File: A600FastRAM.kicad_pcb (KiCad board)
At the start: 2 copper layers, 92.7 x 78.7 mm, 22 parts, among them J1 MC68000_PLCC68, P1 JTAG_CONNECTOR, P98 SCREW_HOLE, P99 OSHW_LOGO, U1 74LS157, U2 74LS157, U3 HYB5118160BSJ, U4 HYB5118160BSJ, U5 ATF1502AS-10JU44

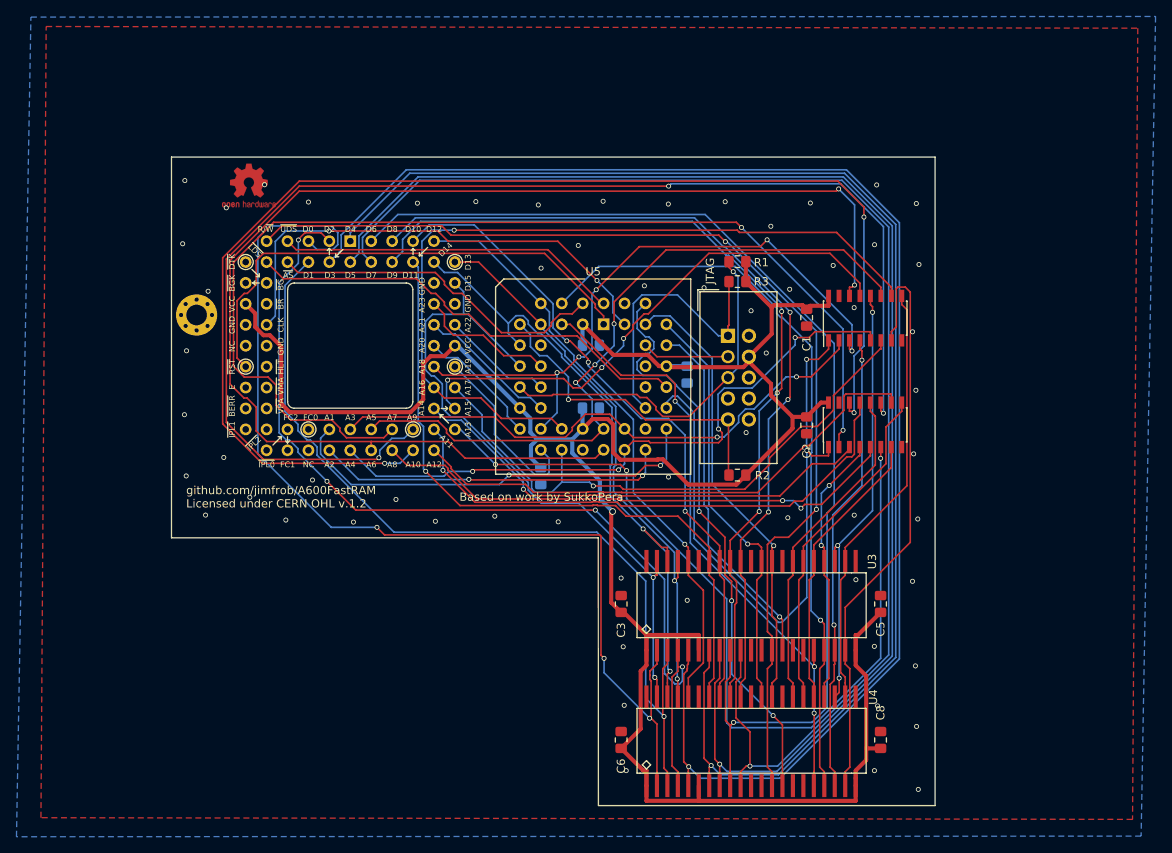
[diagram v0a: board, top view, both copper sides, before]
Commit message: rounded the corners of the PCB
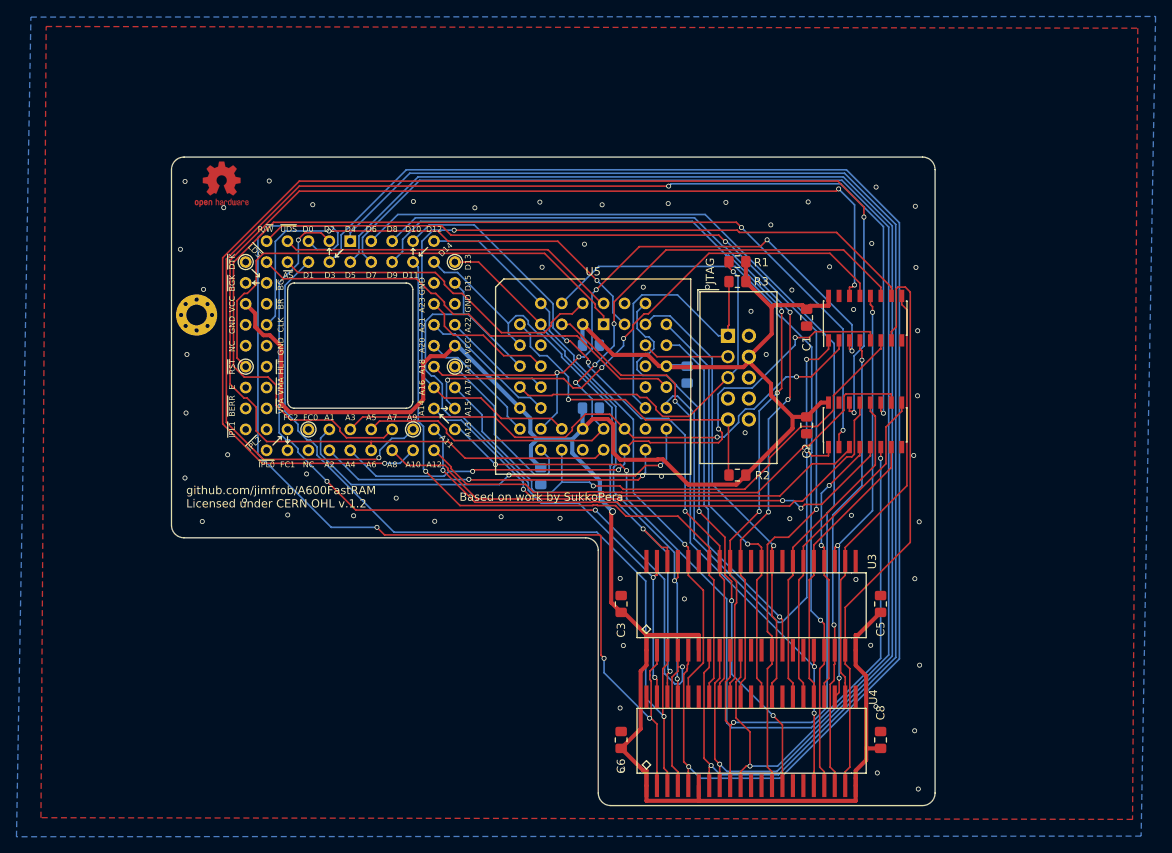
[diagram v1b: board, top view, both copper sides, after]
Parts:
- moved P99 3.31 mm to (117.1, 86.1)
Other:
- outline, holes or cut-outs redrawn

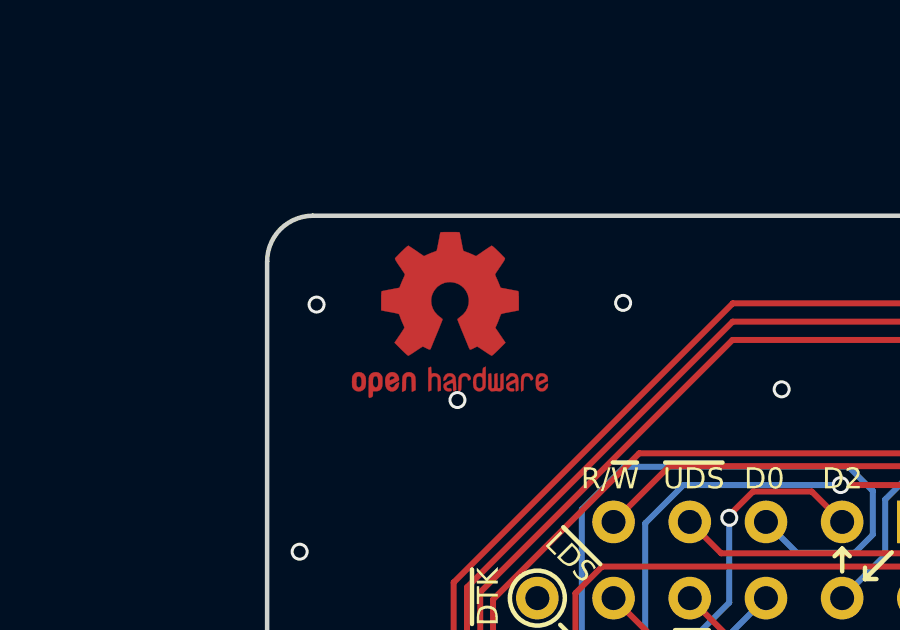
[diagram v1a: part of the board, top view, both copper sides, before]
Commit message: Moved Open Hardware logo to silkscreen
Additionally, the PCB is now a KiCAD 8.0 file
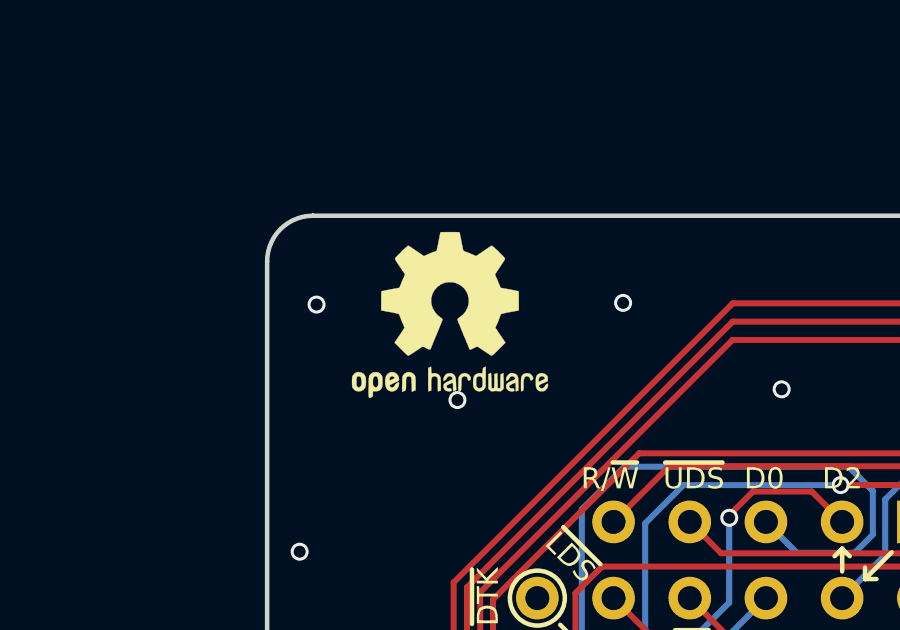
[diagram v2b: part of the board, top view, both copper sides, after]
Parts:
- P99: footprint Symbol:OSHW-Logo2_7.3x6mm_Copper -> Symbol:OSHW-Logo2_7.3x6mm_SilkScreen
